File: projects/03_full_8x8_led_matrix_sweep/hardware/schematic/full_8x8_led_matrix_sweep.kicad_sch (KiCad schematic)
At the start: 10 parts, among them U1 1088B8

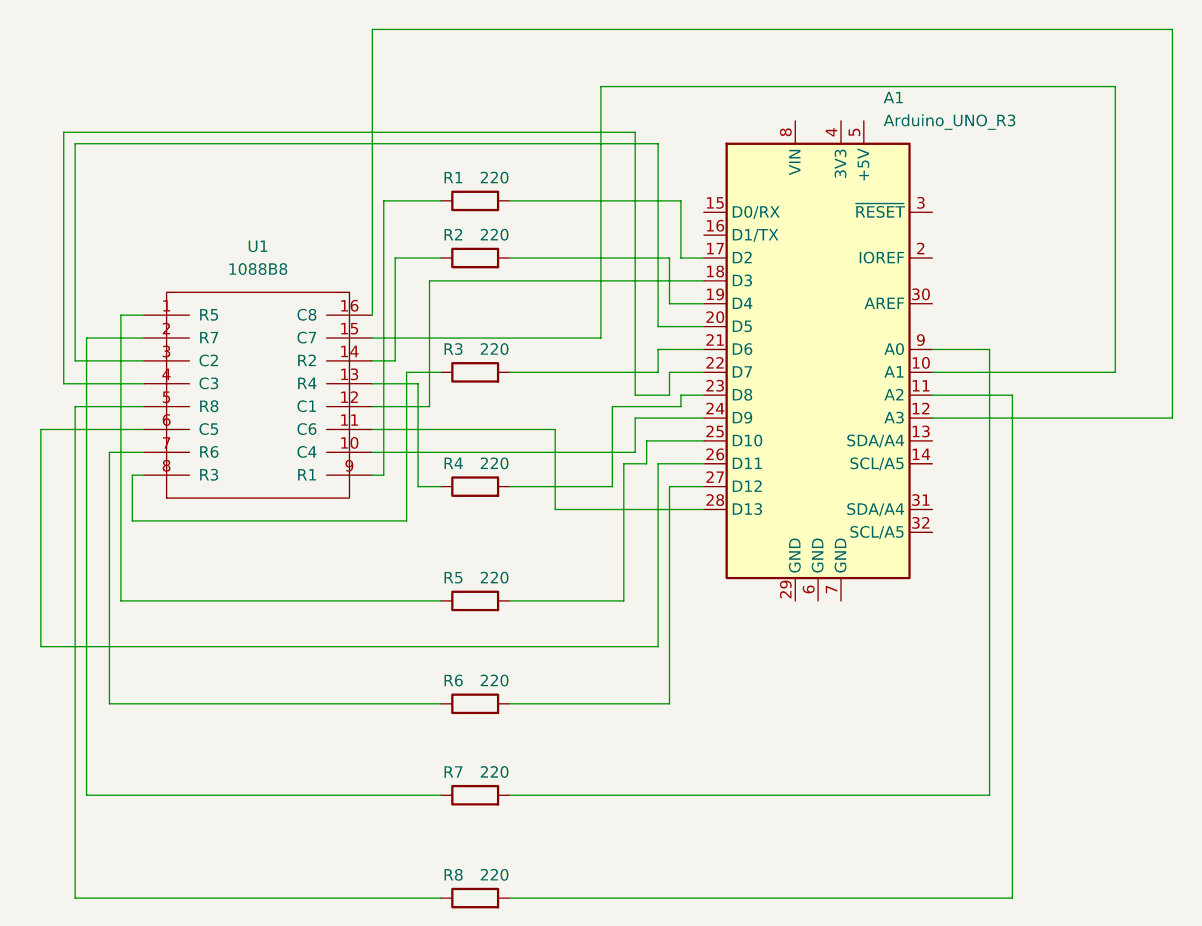
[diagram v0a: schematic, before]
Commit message: docs(hardware): correct circuit schemma
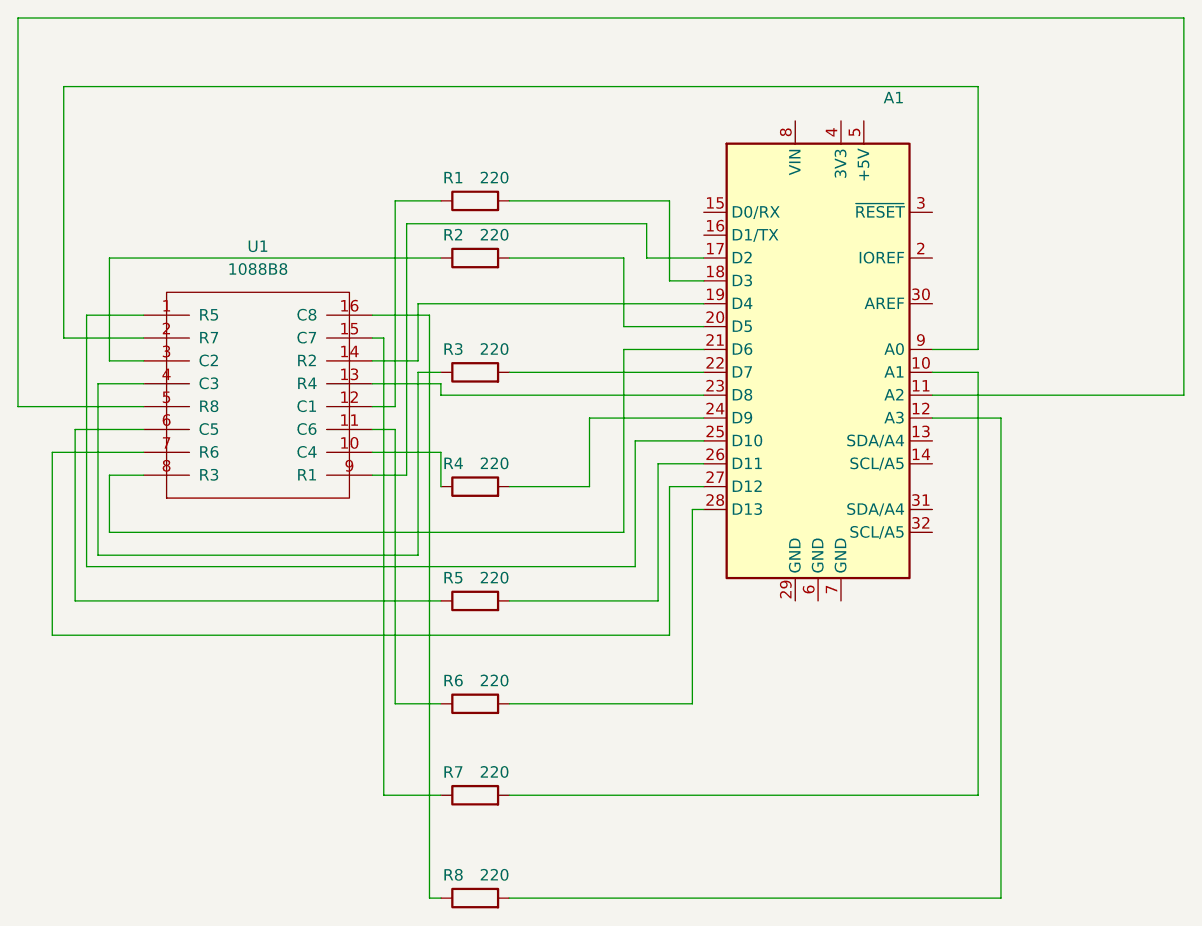
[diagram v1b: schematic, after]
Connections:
- net at R5.1: now also U1.6 (C5); no longer U1.1 (R5)
- net at R5.2: now also A1.26 (D11); no longer A1.25 (D10)
- net at R6.1: now also U1.11 (C6); no longer U1.7 (R6)
- net at R6.2: now also A1.28 (D13); no longer A1.27 (D12)
- net at R7.1: now also U1.15 (C7); no longer U1.2 (R7)
- net at R7.2: now also A1.10 (A1); no longer A1.9 (A0)
- net at R1.1: now also U1.12 (C1); no longer U1.9 (R1)
- net at R1.2: now also A1.18 (D3); no longer A1.17 (D2)
- net at R2.1: now also U1.3 (C2); no longer U1.14 (R2)
- net at R2.2: now also A1.20 (D5); no longer A1.19 (D4)
- net at U1.10 (C4): now also R4.1; no longer A1.24 (D9)
- net at U1.13 (R4): now also A1.23 (D8); no longer R4.1
- net at U1.16 (C8): now also R8.1; no longer A1.12 (A3)
- net at U1.4 (C3): now also R3.1; no longer A1.22 (D7)
- net at U1.5 (R8): now also A1.11 (A2); no longer R8.1
- net at U1.8 (R3): now also A1.21 (D6); no longer R3.1
- net at R8.2: now also A1.12 (A3); no longer A1.11 (A2)
- net at R3.2: now also A1.22 (D7); no longer A1.21 (D6)
- net at R4.2: now also A1.24 (D9); no longer A1.23 (D8)
- new net: A1.25 (D10), U1.1 (R5)
- new net: A1.19 (D4), U1.14 (R2)
- new net: A1.9 (A0), U1.2 (R7)
- new net: A1.27 (D12), U1.7 (R6)
- new net: A1.17 (D2), U1.9 (R1)
